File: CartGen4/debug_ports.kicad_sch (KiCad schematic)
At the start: 3 parts, among them J2 Conn_01x05_Male, J3 Conn_02x10_Odd_Even

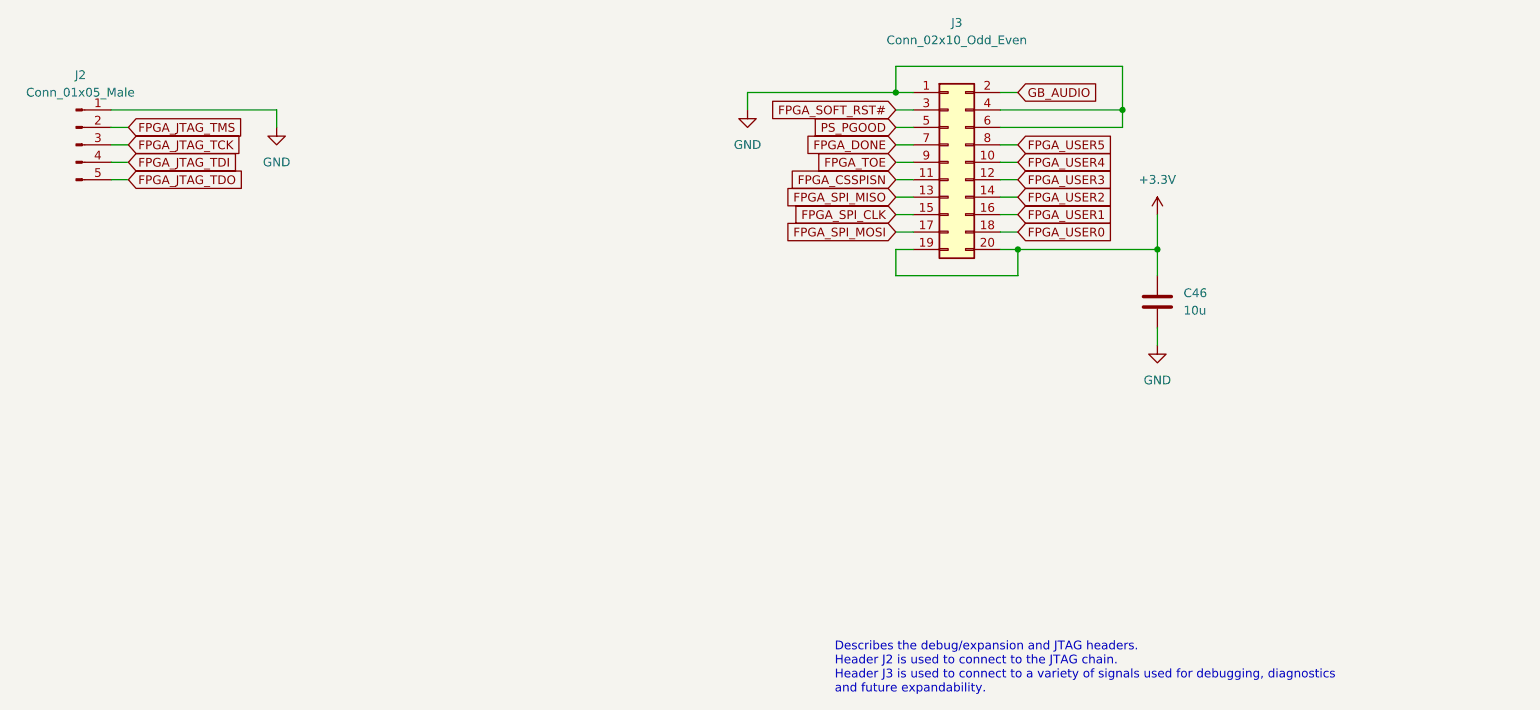
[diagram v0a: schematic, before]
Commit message: Reassigned RD geographically
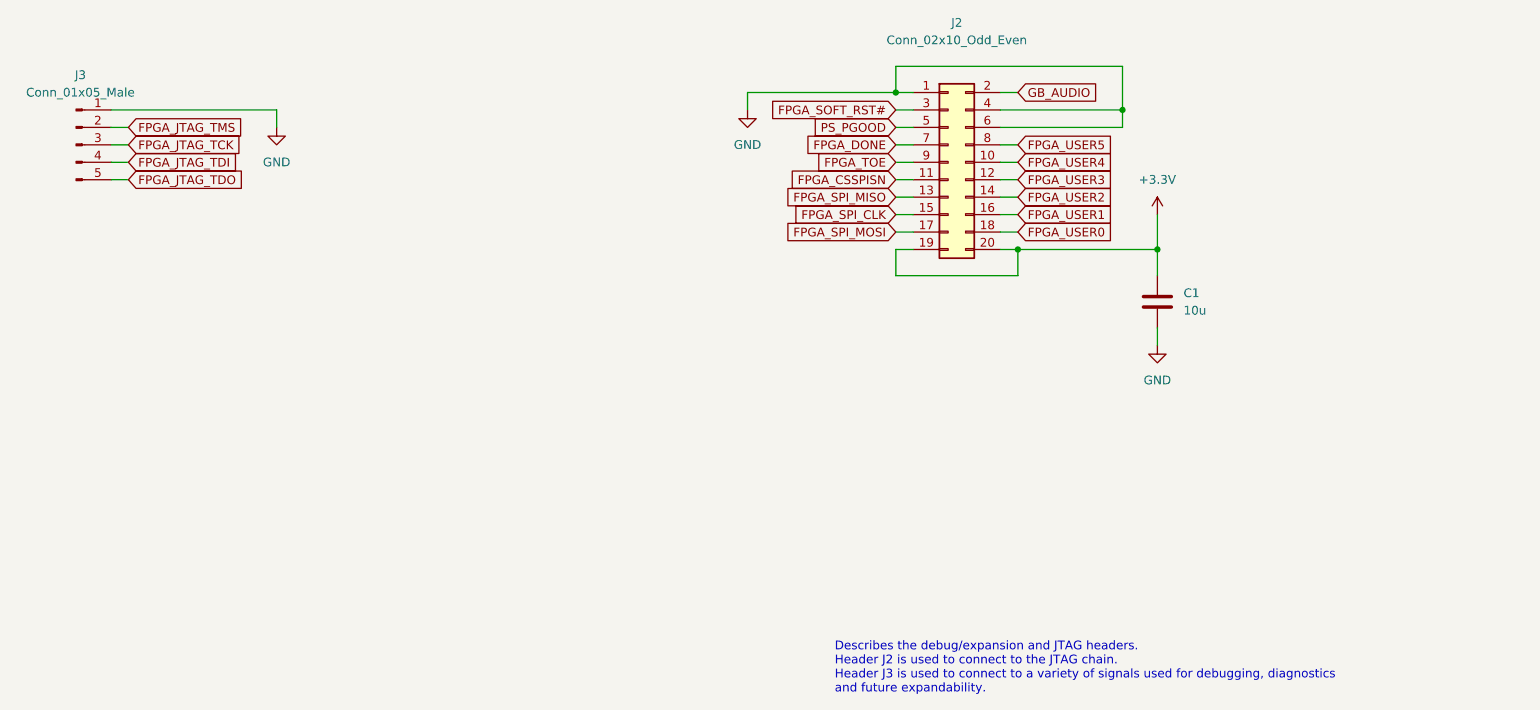
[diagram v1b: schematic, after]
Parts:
- renumbered C46 to C1, J3 to J2, J2 to J3
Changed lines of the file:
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@@
   (symbol (lib_id "Connector_Generic:Conn_02x10_Odd_Even") (at 195.58 97.79 0) (unit 1)
     (in_bom yes) (on_board yes)
-    (property "Reference" "J3" (id 0) (at 196.85 77.47 0))
+    (property "Reference" "J2" (id 0) (at 196.85 77.47 0))
     (property "Value" "Conn_02x10_Odd_Even" (id 1) (at 196.85 80.01 0))
     (property "Footprint" "Connector:Conn_02x10" (id 2) (at 195.58 97.79 0)
@@
   (symbol (lib_id "Device:C") (at 226.06 118.11 0) (unit 1)
     (in_bom yes) (on_board yes) (fields_autoplaced)
-    (property "Reference" "C46" (id 0) (at 229.87 116.8399 0)
+    (property "Reference" "C1" (id 0) (at 229.87 116.8399 0)
       (effects (font (size 1.27 1.27)) (justify left))
     )
@@
   (symbol (lib_id "Connector:Conn_01x05_Male") (at 68.58 95.25 0) (unit 1)
     (in_bom yes) (on_board yes)
-    (property "Reference" "J2" (id 0) (at 69.215 85.09 0))
+    (property "Reference" "J3" (id 0) (at 69.215 85.09 0))
     (property "Value" "Conn_01x05_Male" (id 1) (at 69.215 87.63 0))
     (property "Footprint" "Connector_PinHeader_1.27mm:PinHeader_1x05_P1.27mm_Vertical" (id 2) (at 68.58 95.25 0)

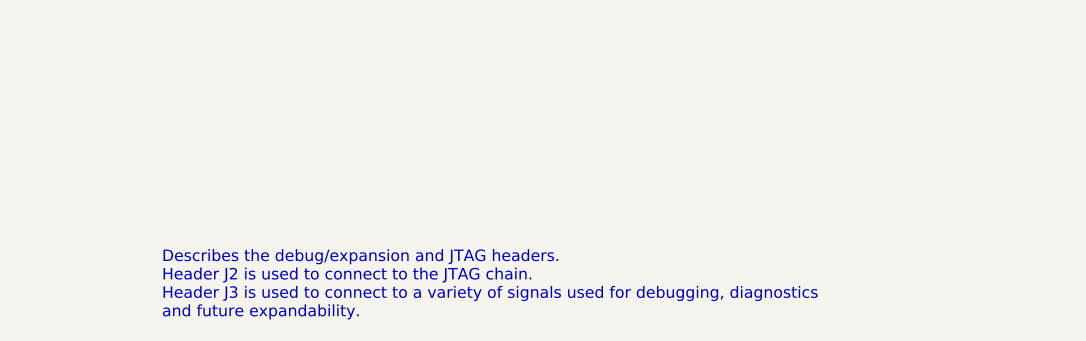
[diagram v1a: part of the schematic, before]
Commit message: Minor fixes to reference designators
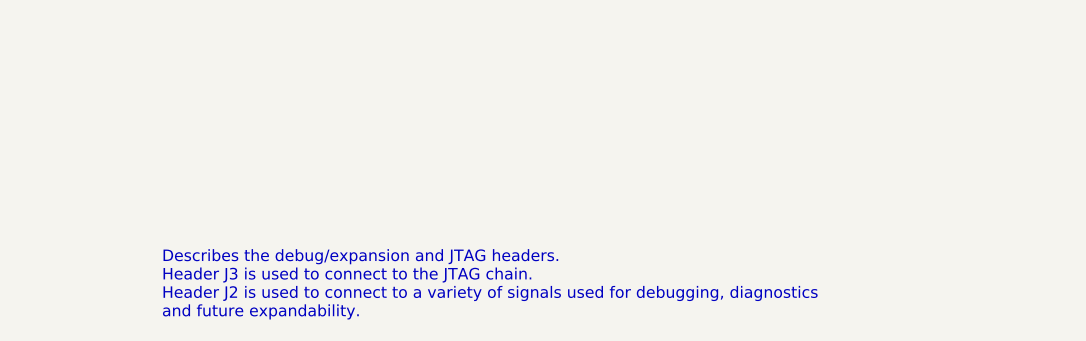
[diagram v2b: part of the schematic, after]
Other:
- note added: "Describes the debug/expansion and JTAG headers. Header J3 is used to connect to the JTAG chain. Header J2 is used to connect to a variety of signals used for debugging, diagnostics and future expandability."
- note removed: "Describes the debug/expansion and JTAG headers. Header J2 is used to connect to the JTAG chain. Header J3 is used to connect to a variety of signals used for debugging, diagnostics and future expandability."
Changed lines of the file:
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@@
     (stroke (width 0) (type default) (color 0 0 0 0))
   )
-  (text "Describes the debug/expansion and JTAG headers.\nHeader J2 is used to connect to the JTAG chain.\nHeader J3 is used to connect to a variety of signals used for debugging, diagnostics\nand future expandability."
+  (text "Describes the debug/expansion and JTAG headers.\nHeader J3 is used to connect to the JTAG chain.\nHeader J2 is used to connect to a variety of signals used for debugging, diagnostics\nand future expandability."
     (at 179.07 175.26 0)
     (effects (font (size 1.27 1.27)) (justify left bottom))
